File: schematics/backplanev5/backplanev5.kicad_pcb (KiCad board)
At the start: 2 copper layers, 150 x 95 mm, 14 parts, among them J11 Conn_01x02, J12 Conn_01x02, J13 Conn_01x02, J14 Conn_01x02

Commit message: Update V1 fabrication 04-12-2025 JLCPCB
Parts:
- added H1: MountingHole, MountingHole:MountingHole_3.2mm_M3, F.Cu at (20.0, 24.9)
- added H2: MountingHole, MountingHole:MountingHole_3.2mm_M3, F.Cu at (20.0, 115.1)
- added H3: MountingHole, MountingHole:MountingHole_3.2mm_M3, F.Cu at (160.1, 115.1)
- added H4: MountingHole, MountingHole:MountingHole_3.2mm_M3, F.Cu at (160.1, 24.9)
- added H5: MountingHole, MountingHole:MountingHole_3.2mm_M3, F.Cu at (90.0, 24.9)
- added H6: MountingHole, MountingHole:MountingHole_3.2mm_M3, F.Cu at (90.0, 115.1)
- moved J11 12.2 mm to (20.5, 41.1)
- moved J14 10.8 mm to (20.5, 45.0)
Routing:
- net GND: track 874.4 -> 863.4 mm
- net /backplane/+5V: track 490.3 -> 499.6 mm
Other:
- board size 150 x 95 mm -> 150 x 100 mm
- board text added: "/BERR"
- board text added: "/BGACK"
- board text added: "/DEN"
- board text added: "/INTA"
- board text added: "/LDS"
- board text added: "/M1"
- board text added: "/RFSH"
- board text added: "/SS0"
- board text added: "/UDS"
- board text added: "/VMA"
- board text added: "/VPA"
- board text added: "/WAIT"
- board text added: "1"
- board text added: "10"
- board text added: "11"
- board text added: "12"
- board text added: "13"
- board text added: "14"
- board text added: "15"
- board text added: "16"
- board text added: "17"
- board text added: "18"
- board text added: "19"
- board text added: "2"
- board text added: "20"
- board text added: "21"
- board text added: "22"
- board text added: "23"
- board text added: "24"
- board text added: "25"
- board text added: "26"
- board text added: "27"
- board text added: "28"
- board text added: "29"
- board text added: "3"
- board text added: "30"
- board text added: "31"
- board text added: "32"
- board text added: "4"
- board text added: "5"
- board text added: "6"
- board text added: "64"
- board text added: "65"
- board text added: "66"
- board text added: "67"
- board text added: "68"
- board text added: "69"
- board text added: "7"
- board text added: "70"
- board text added: "71"
- board text added: "72"
- board text added: "73"
- board text added: "74"
- board text added: "75"
- board text added: "76"
- board text added: "77"
- board text added: "78"
- board text added: "79"
- board text added: "8"
- board text added: "80"
- board text added: "81"
- board text added: "82"
- board text added: "83"
- board text added: "84"
- board text added: "85"
- board text added: "86"
- board text added: "87"
- board text added: "88"
- board text added: "89"
- board text added: "9"
- board text added: "90"
- board text added: "91"
- board text added: "92"
- board text added: "93"
- board text added: "94"
- board text added: "95"
- board text added: "96"
- board text added: "ALE"
- board text added: "DT/R"
- board text added: "M/IO"
- board text added: "Mod: 09CON"
- board text added: "PDSILVA (C)2549"
- board text added: "Res1"
- board text added: "Res10"
- board text added: "Res11"
- board text added: "Res2"
- board text added: "Res3"
- board text added: "Res4"
- board text added: "Res5"
- board text added: "Res6"
- board text added: "Res7"
- board text added: "Res8"
- board text added: "Res9"
- board text added: "Rev: A 2549"
- board text removed: "MULTI-CPU"
- board text removed: "Res"

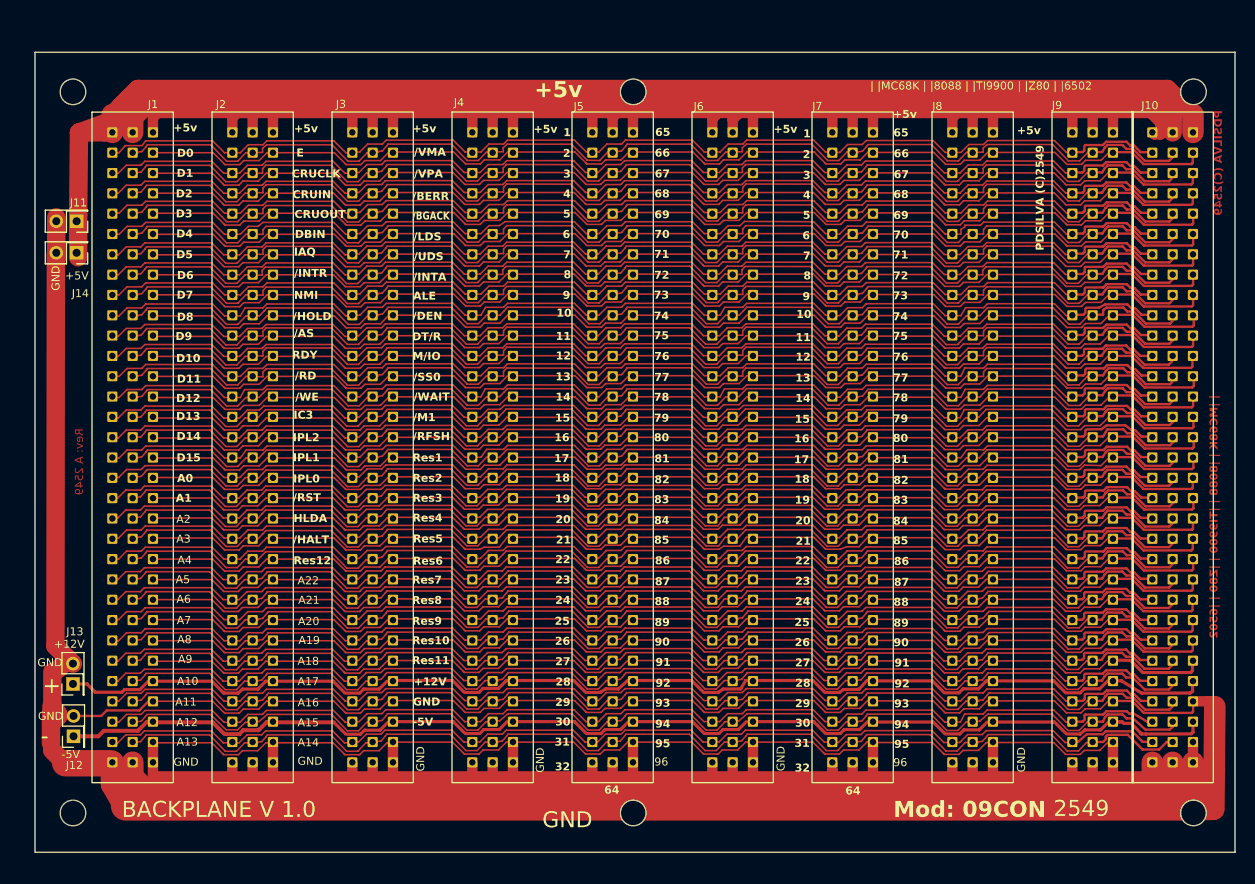
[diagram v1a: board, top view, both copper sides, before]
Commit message: Terminada as mudancas falta agora fazer oDRC
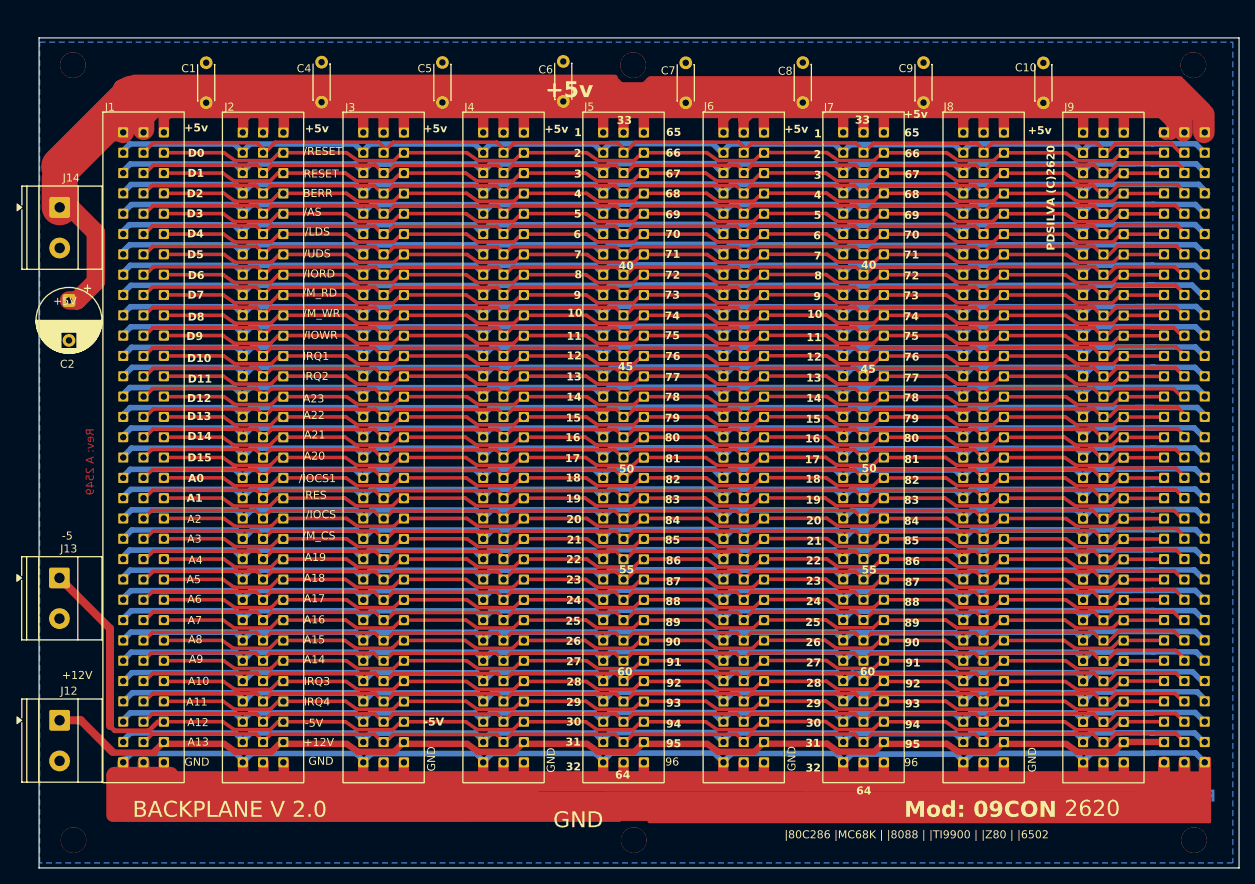
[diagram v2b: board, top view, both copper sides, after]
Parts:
- removed J11: Conn_01x02, Connector_PinHeader_2.54mm:PinHeader_2x01_P2.54mm_Vertical
- added C1: 100nF, Capacitor_THT:C_Disc_D4.3mm_W1.9mm_P5.00mm, F.Cu at (36.6, 26.3)
- added C10: 100nF, Capacitor_THT:C_Disc_D4.3mm_W1.9mm_P5.00mm, F.Cu at (141.3, 26.3)
- added C2: 100uF, Capacitor_THT:CP_Radial_D8.0mm_P5.00mm, F.Cu at (19.5, 51.0)
- added C4: 100nF, Capacitor_THT:C_Disc_D4.3mm_W1.9mm_P5.00mm, F.Cu at (51.1, 26.2)
- added C5: 100nF, Capacitor_THT:C_Disc_D4.3mm_W1.9mm_P5.00mm, F.Cu at (66.2, 26.3)
- added C6: 100nF, Capacitor_THT:C_Disc_D4.3mm_W1.9mm_P5.00mm, F.Cu at (81.3, 26.1)
- added C7: 100nF, Capacitor_THT:C_Disc_D4.3mm_W1.9mm_P5.00mm, F.Cu at (96.6, 26.3)
- added C8: 100nF, Capacitor_THT:C_Disc_D4.3mm_W1.9mm_P5.00mm, F.Cu at (111.2, 26.3)
- added C9: 100nF, Capacitor_THT:C_Disc_D4.3mm_W1.9mm_P5.00mm, F.Cu at (126.3, 26.3)
- J10: moved to B.Cu
- J12, J13, J14: footprint Connector_PinHeader_2.54mm:PinHeader_2x01_P2.54mm_Vertical -> TerminalBlock_Phoenix:TerminalBlock_Phoenix_MKDS-1,5-2-5.08_1x02_P5.08mm_Horizontal
- moved J13 13.4 mm to (18.3, 85.7), turned to -90 degrees
- moved J14 6.06 mm to (18.3, 39.4), turned to -90 degrees
- moved H2 3.40 mm to (20.1, 118.5)
- moved H3 3.40 mm to (160.1, 118.5)
- moved H6 3.40 mm to (90.1, 118.5)
- moved H1 3.34 mm to (20.0, 21.6)
- moved H4 3.34 mm to (160.0, 21.6)
- moved H5 3.34 mm to (90.0, 21.6)
- moved J12 2.65 mm to (18.3, 103.5), turned to -90 degrees
- moved J10 1.47 mm to (158.9, 24.9), turned to 180 degrees
- moved J6 1.39 mm to (103.8, 24.9)
- moved J8 1.37 mm to (133.8, 24.9)
- moved J3 1.37 mm to (58.8, 24.9)
- moved J4 1.36 mm to (73.8, 24.9)
- moved J5 1.36 mm to (88.8, 24.9)
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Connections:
- net /backplane/ALE renamed /backplane//memrd
- net /backplane/CRUCLK renamed /backplane/R2
- net /backplane/CRUIN renamed /backplane/R3
- net /backplane/CRUOUT renamed /backplane/R4
- net /backplane/DBIN renamed /backplane/R5
- net /backplane/DT/R renamed /backplane//iowr
- net /backplane/HLDA renamed /backplane/R19
- net /backplane/IAQ renamed /backplane/R6
- net /backplane/IC3 renamed /backplane/R14
- net /backplane/IPL0 renamed /backplane/R17
- net /backplane/IPL1 renamed /backplane/R16
- net /backplane/IPL2 renamed /backplane/R15
- net /backplane/NMI renamed /backplane/R8
- net /backplane/RDY renamed /backplane/R11
- net /backplane/Res12 renamed /backplane/R21
- net /backplane/Res2 renamed /backplane//IO_CS1
- net /backplane/Res4 renamed /backplane//IO_CS
- net /backplane/Res5 renamed /backplane//MEM_CS
- net /backplane//DEN renamed /backplane//memwr
- net /backplane//HALT renamed /backplane/R20
- net /backplane//HOLD renamed /backplane/R9
- net /backplane//INTA renamed /backplane//iord
- net /backplane//INTR renamed /backplane/R7
- net /backplane//RD renamed /backplane/R12
- net /backplane//RST renamed /backplane/R18
- net /backplane//WAIT renamed /backplane/A23
- net /backplane//WE renamed /backplane/R13
- J1 pad 34: /backplane/E -> /backplane/R1
- J1 pad 43: /backplane//AS -> /backplane/R10
- J1 pad 55: /backplane/A22 -> /backplane/R22
- J1 pad 56: /backplane/A21 -> /backplane/R23
- J1 pad 57: /backplane/A20 -> /backplane/R24
- J1 pad 58: /backplane/A19 -> /backplane/R25
- J1 pad 59: /backplane/A18 -> /backplane/R26
- J1 pad 60: /backplane/A17 -> /backplane/R27
- J1 pad 61: /backplane/A16 -> /backplane/R28
- J1 pad 62: /backplane/A15 -> /backplane/R29
- J1 pad 63: /backplane/A14 -> /backplane/R30
- J1 pad 66: /backplane//VMA -> /backplane//RESET
- J1 pad 67: /backplane//VPA -> /backplane/RESET
- J1 pad 69: /backplane//BGACK -> /backplane//AS
- J1 pad 76: /backplane/M/IO -> /backplane//VMA
- J1 pad 77: /backplane//SSO -> /backplane//VPA
- J1 pad 79: /backplane//M1 -> /backplane/A22
- J1 pad 80: /backplane//RFSH -> /backplane/A21
- J1 pad 81: /backplane/Res1 -> /backplane/A20
- J1 pad 83: /backplane/Res3 -> /backplane/E
- J1 pad 86: /backplane/Res6 -> /backplane/A19
- J1 pad 87: /backplane/Res7 -> /backplane/A18
- J1 pad 88: /backplane/Res8 -> /backplane/A17
- J1 pad 89: /backplane/Res9 -> /backplane/A16
- J1 pad 90: /backplane/Res10 -> /backplane/A15
- J1 pad 91: /backplane/Res11 -> /backplane/A14
- J1 pad 92: /backplane/+12V -> /backplane/R31
- J1 pad 93: GND -> /backplane/R32
- J1 pad 95: GND -> /backplane/+12V
- J10 pad 34: /backplane/E -> /backplane/R1
- J10 pad 43: /backplane//AS -> /backplane/R10
- J10 pad 55: /backplane/A22 -> /backplane/R22
- J10 pad 56: /backplane/A21 -> /backplane/R23
- J10 pad 57: /backplane/A20 -> /backplane/R24
- J10 pad 58: /backplane/A19 -> /backplane/R25
- J10 pad 59: /backplane/A18 -> /backplane/R26
- J10 pad 60: /backplane/A17 -> /backplane/R27
- J10 pad 61: /backplane/A16 -> /backplane/R28
- J10 pad 62: /backplane/A15 -> /backplane/R29
- J10 pad 63: /backplane/A14 -> /backplane/R30
- J10 pad 66: /backplane//VMA -> /backplane//RESET
- J10 pad 67: /backplane//VPA -> /backplane/RESET
- J10 pad 69: /backplane//BGACK -> /backplane//AS
- J10 pad 76: /backplane/M/IO -> /backplane//VMA
- J10 pad 77: /backplane//SSO -> /backplane//VPA
- J10 pad 79: /backplane//M1 -> /backplane/A22
- J10 pad 80: /backplane//RFSH -> /backplane/A21
- J10 pad 81: /backplane/Res1 -> /backplane/A20
- J10 pad 83: /backplane/Res3 -> /backplane/E
- J10 pad 86: /backplane/Res6 -> /backplane/A19
- J10 pad 87: /backplane/Res7 -> /backplane/A18
- J10 pad 88: /backplane/Res8 -> /backplane/A17
- J10 pad 89: /backplane/Res9 -> /backplane/A16
- J10 pad 90: /backplane/Res10 -> /backplane/A15
- J10 pad 91: /backplane/Res11 -> /backplane/A14
- J10 pad 92: /backplane/+12V -> /backplane/R31
- J10 pad 93: GND -> /backplane/R32
- J10 pad 95: GND -> /backplane/+12V
- J12 pad 1: /backplane/-5V -> /backplane/+12V
- J13 pad 1: /backplane/+12V -> /backplane/-5V
- J2 pad 34: /backplane/E -> /backplane/R1
- J2 pad 43: /backplane//AS -> /backplane/R10
- J2 pad 55: /backplane/A22 -> /backplane/R22
- J2 pad 56: /backplane/A21 -> /backplane/R23
- J2 pad 57: /backplane/A20 -> /backplane/R24
- J2 pad 58: /backplane/A19 -> /backplane/R25
- J2 pad 59: /backplane/A18 -> /backplane/R26
- J2 pad 60: /backplane/A17 -> /backplane/R27
- J2 pad 61: /backplane/A16 -> /backplane/R28
- J2 pad 62: /backplane/A15 -> /backplane/R29
- J2 pad 63: /backplane/A14 -> /backplane/R30
- J2 pad 66: /backplane//VMA -> /backplane//RESET
- J2 pad 67: /backplane//VPA -> /backplane/RESET
- J2 pad 69: /backplane//BGACK -> /backplane//AS
- J2 pad 76: /backplane/M/IO -> /backplane//VMA
- J2 pad 77: /backplane//SSO -> /backplane//VPA
- J2 pad 79: /backplane//M1 -> /backplane/A22
- J2 pad 80: /backplane//RFSH -> /backplane/A21
- J2 pad 81: /backplane/Res1 -> /backplane/A20
- J2 pad 83: /backplane/Res3 -> /backplane/E
- J2 pad 86: /backplane/Res6 -> /backplane/A19
- J2 pad 87: /backplane/Res7 -> /backplane/A18
- J2 pad 88: /backplane/Res8 -> /backplane/A17
- J2 pad 89: /backplane/Res9 -> /backplane/A16
- J2 pad 90: /backplane/Res10 -> /backplane/A15
- J2 pad 91: /backplane/Res11 -> /backplane/A14
- J2 pad 92: /backplane/+12V -> /backplane/R31
- J2 pad 93: GND -> /backplane/R32
- J2 pad 95: GND -> /backplane/+12V
- J3 pad 34: /backplane/E -> /backplane/R1
- J3 pad 43: /backplane//AS -> /backplane/R10
- J3 pad 55: /backplane/A22 -> /backplane/R22
- J3 pad 56: /backplane/A21 -> /backplane/R23
- J3 pad 57: /backplane/A20 -> /backplane/R24
- J3 pad 58: /backplane/A19 -> /backplane/R25
- J3 pad 59: /backplane/A18 -> /backplane/R26
- J3 pad 60: /backplane/A17 -> /backplane/R27
- J3 pad 61: /backplane/A16 -> /backplane/R28
- J3 pad 62: /backplane/A15 -> /backplane/R29
- J3 pad 63: /backplane/A14 -> /backplane/R30
- J3 pad 66: /backplane//VMA -> /backplane//RESET
- J3 pad 67: /backplane//VPA -> /backplane/RESET
- J3 pad 69: /backplane//BGACK -> /backplane//AS
- J3 pad 76: /backplane/M/IO -> /backplane//VMA
- J3 pad 77: /backplane//SSO -> /backplane//VPA
- J3 pad 79: /backplane//M1 -> /backplane/A22
- J3 pad 80: /backplane//RFSH -> /backplane/A21
- J3 pad 81: /backplane/Res1 -> /backplane/A20
- J3 pad 83: /backplane/Res3 -> /backplane/E
- J3 pad 86: /backplane/Res6 -> /backplane/A19
- J3 pad 87: /backplane/Res7 -> /backplane/A18
- J3 pad 88: /backplane/Res8 -> /backplane/A17
- J3 pad 89: /backplane/Res9 -> /backplane/A16
- J3 pad 90: /backplane/Res10 -> /backplane/A15
- J3 pad 91: /backplane/Res11 -> /backplane/A14
- J3 pad 92: /backplane/+12V -> /backplane/R31
- J3 pad 93: GND -> /backplane/R32
- J3 pad 95: GND -> /backplane/+12V
- J4 pad 34: /backplane/E -> /backplane/R1
- J4 pad 43: /backplane//AS -> /backplane/R10
- J4 pad 55: /backplane/A22 -> /backplane/R22
- J4 pad 56: /backplane/A21 -> /backplane/R23
- J4 pad 57: /backplane/A20 -> /backplane/R24
- J4 pad 58: /backplane/A19 -> /backplane/R25
- J4 pad 59: /backplane/A18 -> /backplane/R26
- J4 pad 60: /backplane/A17 -> /backplane/R27
- J4 pad 61: /backplane/A16 -> /backplane/R28
- J4 pad 62: /backplane/A15 -> /backplane/R29
- J4 pad 63: /backplane/A14 -> /backplane/R30
- J4 pad 66: /backplane//VMA -> /backplane//RESET
- J4 pad 67: /backplane//VPA -> /backplane/RESET
- J4 pad 69: /backplane//BGACK -> /backplane//AS
- J4 pad 76: /backplane/M/IO -> /backplane//VMA
- J4 pad 77: /backplane//SSO -> /backplane//VPA
- J4 pad 79: /backplane//M1 -> /backplane/A22
- J4 pad 80: /backplane//RFSH -> /backplane/A21
- J4 pad 81: /backplane/Res1 -> /backplane/A20
- J4 pad 83: /backplane/Res3 -> /backplane/E
- J4 pad 86: /backplane/Res6 -> /backplane/A19
- J4 pad 87: /backplane/Res7 -> /backplane/A18
- J4 pad 88: /backplane/Res8 -> /backplane/A17
- J4 pad 89: /backplane/Res9 -> /backplane/A16
- J4 pad 90: /backplane/Res10 -> /backplane/A15
- J4 pad 91: /backplane/Res11 -> /backplane/A14
- J4 pad 92: /backplane/+12V -> /backplane/R31
- J4 pad 93: GND -> /backplane/R32
- J4 pad 95: GND -> /backplane/+12V
- J5 pad 34: /backplane/E -> /backplane/R1
- J5 pad 43: /backplane//AS -> /backplane/R10
- J5 pad 55: /backplane/A22 -> /backplane/R22
- J5 pad 56: /backplane/A21 -> /backplane/R23
- J5 pad 57: /backplane/A20 -> /backplane/R24
- J5 pad 58: /backplane/A19 -> /backplane/R25
- J5 pad 59: /backplane/A18 -> /backplane/R26
- J5 pad 60: /backplane/A17 -> /backplane/R27
- J5 pad 61: /backplane/A16 -> /backplane/R28
- J5 pad 62: /backplane/A15 -> /backplane/R29
- J5 pad 63: /backplane/A14 -> /backplane/R30
- J5 pad 66: /backplane//VMA -> /backplane//RESET
- J5 pad 67: /backplane//VPA -> /backplane/RESET
- J5 pad 69: /backplane//BGACK -> /backplane//AS
- J5 pad 76: /backplane/M/IO -> /backplane//VMA
- J5 pad 77: /backplane//SSO -> /backplane//VPA
- J5 pad 79: /backplane//M1 -> /backplane/A22
- J5 pad 80: /backplane//RFSH -> /backplane/A21
- J5 pad 81: /backplane/Res1 -> /backplane/A20
- J5 pad 83: /backplane/Res3 -> /backplane/E
- J5 pad 86: /backplane/Res6 -> /backplane/A19
- J5 pad 87: /backplane/Res7 -> /backplane/A18
- J5 pad 88: /backplane/Res8 -> /backplane/A17
- J5 pad 89: /backplane/Res9 -> /backplane/A16
- J5 pad 90: /backplane/Res10 -> /backplane/A15
- J5 pad 91: /backplane/Res11 -> /backplane/A14
- J5 pad 92: /backplane/+12V -> /backplane/R31
- J5 pad 93: GND -> /backplane/R32
- J5 pad 95: GND -> /backplane/+12V
- J6 pad 34: /backplane/E -> /backplane/R1
- J6 pad 43: /backplane//AS -> /backplane/R10
- J6 pad 55: /backplane/A22 -> /backplane/R22
- J6 pad 56: /backplane/A21 -> /backplane/R23
- J6 pad 57: /backplane/A20 -> /backplane/R24
- J6 pad 58: /backplane/A19 -> /backplane/R25
- J6 pad 59: /backplane/A18 -> /backplane/R26
- J6 pad 60: /backplane/A17 -> /backplane/R27
- J6 pad 61: /backplane/A16 -> /backplane/R28
- J6 pad 62: /backplane/A15 -> /backplane/R29
- J6 pad 63: /backplane/A14 -> /backplane/R30
- J6 pad 66: /backplane//VMA -> /backplane//RESET
- J6 pad 67: /backplane//VPA -> /backplane/RESET
- J6 pad 69: /backplane//BGACK -> /backplane//AS
- J6 pad 76: /backplane/M/IO -> /backplane//VMA
- J6 pad 77: /backplane//SSO -> /backplane//VPA
- J6 pad 79: /backplane//M1 -> /backplane/A22
- J6 pad 80: /backplane//RFSH -> /backplane/A21
- J6 pad 81: /backplane/Res1 -> /backplane/A20
- J6 pad 83: /backplane/Res3 -> /backplane/E
- J6 pad 86: /backplane/Res6 -> /backplane/A19
- J6 pad 87: /backplane/Res7 -> /backplane/A18
- J6 pad 88: /backplane/Res8 -> /backplane/A17
- J6 pad 89: /backplane/Res9 -> /backplane/A16
- J6 pad 90: /backplane/Res10 -> /backplane/A15
- J6 pad 91: /backplane/Res11 -> /backplane/A14
- J6 pad 92: /backplane/+12V -> /backplane/R31
- J6 pad 93: GND -> /backplane/R32
- J6 pad 95: GND -> /backplane/+12V
- J7 pad 34: /backplane/E -> /backplane/R1
- J7 pad 43: /backplane//AS -> /backplane/R10
- J7 pad 55: /backplane/A22 -> /backplane/R22
- J7 pad 56: /backplane/A21 -> /backplane/R23
- J7 pad 57: /backplane/A20 -> /backplane/R24
- J7 pad 58: /backplane/A19 -> /backplane/R25
- J7 pad 59: /backplane/A18 -> /backplane/R26
- J7 pad 60: /backplane/A17 -> /backplane/R27
- J7 pad 61: /backplane/A16 -> /backplane/R28
- J7 pad 62: /backplane/A15 -> /backplane/R29
- J7 pad 63: /backplane/A14 -> /backplane/R30
- J7 pad 66: /backplane//VMA -> /backplane//RESET
- J7 pad 67: /backplane//VPA -> /backplane/RESET
- J7 pad 69: /backplane//BGACK -> /backplane//AS
- J7 pad 76: /backplane/M/IO -> /backplane//VMA
- J7 pad 77: /backplane//SSO -> /backplane//VPA
- J7 pad 79: /backplane//M1 -> /backplane/A22
- J7 pad 80: /backplane//RFSH -> /backplane/A21
- J7 pad 81: /backplane/Res1 -> /backplane/A20
- J7 pad 83: /backplane/Res3 -> /backplane/E
- J7 pad 86: /backplane/Res6 -> /backplane/A19
- J7 pad 87: /backplane/Res7 -> /backplane/A18
- J7 pad 88: /backplane/Res8 -> /backplane/A17
- J7 pad 89: /backplane/Res9 -> /backplane/A16
- J7 pad 90: /backplane/Res10 -> /backplane/A15
- J7 pad 91: /backplane/Res11 -> /backplane/A14
- J7 pad 92: /backplane/+12V -> /backplane/R31
- J7 pad 93: GND -> /backplane/R32
- J7 pad 95: GND -> /backplane/+12V
- J8 pad 34: /backplane/E -> /backplane/R1
- J8 pad 43: /backplane//AS -> /backplane/R10
- J8 pad 55: /backplane/A22 -> /backplane/R22
- J8 pad 56: /backplane/A21 -> /backplane/R23
- J8 pad 57: /backplane/A20 -> /backplane/R24
- J8 pad 58: /backplane/A19 -> /backplane/R25
- J8 pad 59: /backplane/A18 -> /backplane/R26
- J8 pad 60: /backplane/A17 -> /backplane/R27
- J8 pad 61: /backplane/A16 -> /backplane/R28
- J8 pad 62: /backplane/A15 -> /backplane/R29
- J8 pad 63: /backplane/A14 -> /backplane/R30
- J8 pad 66: /backplane//VMA -> /backplane//RESET
- J8 pad 67: /backplane//VPA -> /backplane/RESET
- J8 pad 69: /backplane//BGACK -> /backplane//AS
- J8 pad 76: /backplane/M/IO -> /backplane//VMA
- J8 pad 77: /backplane//SSO -> /backplane//VPA
- J8 pad 79: /backplane//M1 -> /backplane/A22
- J8 pad 80: /backplane//RFSH -> /backplane/A21
- J8 pad 81: /backplane/Res1 -> /backplane/A20
- J8 pad 83: /backplane/Res3 -> /backplane/E
- J8 pad 86: /backplane/Res6 -> /backplane/A19
- J8 pad 87: /backplane/Res7 -> /backplane/A18
- J8 pad 88: /backplane/Res8 -> /backplane/A17
- J8 pad 89: /backplane/Res9 -> /backplane/A16
- J8 pad 90: /backplane/Res10 -> /backplane/A15
- J8 pad 91: /backplane/Res11 -> /backplane/A14
- J8 pad 92: /backplane/+12V -> /backplane/R31
- J8 pad 93: GND -> /backplane/R32
- J8 pad 95: GND -> /backplane/+12V
- J9 pad 34: /backplane/E -> /backplane/R1
- J9 pad 43: /backplane//AS -> /backplane/R10
- J9 pad 55: /backplane/A22 -> /backplane/R22
- J9 pad 56: /backplane/A21 -> /backplane/R23
- J9 pad 57: /backplane/A20 -> /backplane/R24
- J9 pad 58: /backplane/A19 -> /backplane/R25
- J9 pad 59: /backplane/A18 -> /backplane/R26
- J9 pad 60: /backplane/A17 -> /backplane/R27
- J9 pad 61: /backplane/A16 -> /backplane/R28
- J9 pad 62: /backplane/A15 -> /backplane/R29
- J9 pad 63: /backplane/A14 -> /backplane/R30
- J9 pad 66: /backplane//VMA -> /backplane//RESET
- J9 pad 67: /backplane//VPA -> /backplane/RESET
- J9 pad 69: /backplane//BGACK -> /backplane//AS
- J9 pad 76: /backplane/M/IO -> /backplane//VMA
- J9 pad 77: /backplane//SSO -> /backplane//VPA
- J9 pad 79: /backplane//M1 -> /backplane/A22
- J9 pad 80: /backplane//RFSH -> /backplane/A21
- J9 pad 81: /backplane/Res1 -> /backplane/A20
- J9 pad 83: /backplane/Res3 -> /backplane/E
- J9 pad 86: /backplane/Res6 -> /backplane/A19
- J9 pad 87: /backplane/Res7 -> /backplane/A18
- J9 pad 88: /backplane/Res8 -> /backplane/A17
- J9 pad 89: /backplane/Res9 -> /backplane/A16
- J9 pad 90: /backplane/Res10 -> /backplane/A15
- J9 pad 91: /backplane/Res11 -> /backplane/A14
- J9 pad 92: /backplane/+12V -> /backplane/R31
- J9 pad 93: GND -> /backplane/R32
- J9 pad 95: GND -> /backplane/+12V
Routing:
- net GND: track 863.4 -> 598.4 mm
- net /backplane/Res1: track 141.9 -> 0.00 mm
- net /backplane/Res3: track 141.9 -> 0.00 mm
- net /backplane/Res10: track 141.9 -> 0.00 mm
- net /backplane/M/IO: track 141.9 -> 0.00 mm
- net /backplane/Res9: track 141.9 -> 0.00 mm
- net /backplane/Res8: track 141.9 -> 0.00 mm
- net /backplane//SSO: track 141.9 -> 0.00 mm
- net /backplane//RFSH: track 141.9 -> 0.00 mm
- net /backplane//BGACK: track 141.9 -> 0.00 mm
- net /backplane/Res7: track 141.9 -> 0.00 mm
- net /backplane/Res6: track 141.9 -> 0.00 mm
- net /backplane//M1: track 141.9 -> 0.00 mm
- net /backplane/Res11: track 141.8 -> 0.00 mm
- net /backplane/R1: track 0.00 -> 138.9 mm
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- added copper zone on B.Cu, net GND
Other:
- board size 150 x 100 mm -> 150 x 103.8 mm
- board text added: "-5"
- board text added: "/IOCS"
- board text added: "/IOCS1"
- board text added: "/IORD"
- board text added: "/IOWR"
- board text added: "/M_CS"
- board text added: "/M_RD"
- board text added: "/M_WR"
- board text added: "/RESET"
- board text added: "2620"
- board text added: "33"
- board text added: "40"
- board text added: "45"
- board text added: "50"
- board text added: "55"
- board text added: "60"
- board text added: "A23"
- board text added: "BACKPLANE V 2.0"
- board text added: "BERR"
- board text added: "IRQ1"
- board text added: "IRQ2"
- board text added: "IRQ3"
- board text added: "IRQ4"
- board text added: "PDSILVA (C)2620"
- board text added: "RES"
- board text added: "RESET"
- board text added: "REV.B"
- board text added: "pdsilva 2620"
- board text added: "|80C286 |MC68K | |8088 | |TI9900 | |Z80 | |6502"
- board text removed: "+"
- board text removed: "-"
- board text removed: "/BERR"
- board text removed: "/BGACK"
- board text removed: "/DEN"
- board text removed: "/HALT"
- board text removed: "/HOLD"
- board text removed: "/INTA"
- board text removed: "/INTR"
- board text removed: "/M1"
- board text removed: "/RD"
- board text removed: "/RFSH"
- board text removed: "/RST"
- board text removed: "/SS0"
- board text removed: "/VMA"
- board text removed: "/VPA"
- board text removed: "/WAIT"
- board text removed: "/WE"
- board text removed: "2549"
- board text removed: "ALE"
- board text removed: "BACKPLANE V 1.0"
- board text removed: "CRUCLK"
- board text removed: "CRUIN"
- board text removed: "CRUOUT"
- board text removed: "DBIN"
- board text removed: "DT/R"
- board text removed: "E"
- board text removed: "HLDA"
- board text removed: "IAQ"
- board text removed: "IC3"
- board text removed: "IPL0"
- board text removed: "IPL1"
- board text removed: "IPL2"
- board text removed: "M/IO"
- board text removed: "NMI"
- board text removed: "PDSILVA (C)2549"
- board text removed: "RDY"
- board text removed: "Res1"
- board text removed: "Res10"
- board text removed: "Res11"
- board text removed: "Res12"
- board text removed: "Res2"
- board text removed: "Res3"
- board text removed: "Res4"
- board text removed: "Res5"
- board text removed: "Res6"
- board text removed: "Res7"
- board text removed: "Res8"
- board text removed: "Res9"
- board text removed: "| |MC68K | |8088 | |TI9900 | |Z80 | |6502"

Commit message: Terminado o DRC
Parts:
- moved J12 17.8 mm to (18.3, 85.7)
- moved J13 17.8 mm to (18.3, 103.4)
- moved C4 0.47 mm to (51.5, 26.5)
- moved J14 0.07 mm to (18.3, 39.4)
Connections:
- C4 pad 1: unconnected-(C4-Pad1) -> /backplane/+5V
- C4 pad 2: unconnected-(C4-Pad2) -> GND
- C5 pad 1: unconnected-(C5-Pad1) -> /backplane/+5V
- C5 pad 2: unconnected-(C5-Pad2) -> GND
- J12 pad 1: /backplane/+12V -> /backplane/-5V
- J13 pad 1: /backplane/-5V -> /backplane/+12V
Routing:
- net /backplane/+5V: track 506.5 -> 236.4 mm
- net /backplane/A8: track 142.4 -> 145.1 mm
- net /backplane/A10: track 143.0 -> 145.6 mm
- net /backplane/A9: track 142.7 -> 145.1 mm
- net /backplane/A11: track 142.7 -> 145.0 mm
- net /backplane/D8: track 142.7 -> 144.4 mm
- net /backplane/A12: track 142.7 -> 144.4 mm
- net /backplane/D10: track 142.7 -> 144.3 mm
- net /backplane/D11: track 142.7 -> 144.0 mm
- net /backplane/A0: track 142.7 -> 144.0 mm
- net /backplane/A2: track 142.7 -> 144.0 mm
- net /backplane/D9: track 142.7 -> 144.0 mm
- net /backplane/A13: track 142.7 -> 143.9 mm
- net /backplane/D12: track 142.7 -> 143.9 mm
- net /backplane/A3: track 142.7 -> 143.8 mm
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- added copper zone on F.Cu, net /backplane/+5V
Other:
- board size 150 x 103.8 mm -> 150 x 102.7 mm

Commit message: Versao em producao
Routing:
- net /backplane/+5V: track 236.4 -> 240.3 mm
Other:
- board text added: "Mod: PDS112 09CON"
- board text added: "Rev: B 2620"
- board text added: "SN:"
- board text removed: "Mod: 09CON"
- board text removed: "Rev: A 2549"
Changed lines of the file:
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@@
 		(tenting front back)
 		(pcbplotparams
-			(layerselection 0x00000000_00000000_55555555_575555ff)
+			(layerselection 0x00000000_00000000_55555555_5755557f)
 			(plot_on_all_layers_selection 0x00000000_00000000_00000000_00000000)
 			(disableapertmacros no)
@@
 	)
 	(gr_rect
+		(start 56.43 116.27)
+		(end 79.24 119.34)
+		(stroke
+			(width 0.1)
+			(type default)
+		)
+		(fill no)
+		(layer "F.SilkS")
+	)
+	(gr_rect
 		(start 15.06 18.6964)
 		(end 165.03 121.3556)
@@
 		(layer "Edge.Cuts")
 	)
-	(gr_text "Rev: A 2549"
+	(gr_text "Rev: B 2620"
 		(at 22.72 66.99 90)
 		(layer "F.Cu")
@@
 		)
 	)
-	(gr_text "64"
-		(at 87.76 110.89 0)
+	(gr_text "45\n"
+		(at 87.58 59.85 0)
 		(layer "F.SilkS")
 		(effects
@@
 		)
 	)
-	(gr_text "33"
-		(at 87.97 29.07 0)
+	(gr_text "40"
+		(at 87.64 47.16 0)
 		(layer "F.SilkS")
 		(effects
@@
 	)
 	(gr_text "60\n"
-		(at 88.04 98.01 0)
+		(at 87.66 97.93 0)
 		(layer "F.SilkS")
 		(effects
@@
 		)
 	)
-	(gr_text "45\n"
-		(at 88.12 59.85 0)
+	(gr_text "50"
+		(at 87.73 72.57 0)
 		(layer "F.SilkS")
 		(effects
@@
 		)
 	)
-	(gr_text "40"
-		(at 88.2 47.26 0)
+	(gr_text "64"
+		(at 87.76 110.89 0)
 		(layer "F.SilkS")
 		(effects
@@
 		)
 	)
-	(gr_text "50"
-		(at 88.25 72.65 0)
+	(gr_text "33"
+		(at 87.97 29.07 0)
 		(layer "F.SilkS")
 		(effects
@@
 		)
 	)
-	(gr_text "33"
-		(at 117.73 29.02 0)
+	(gr_text "45\n"
+		(at 117.52 59.86 0)
 		(layer "F.SilkS")
 		(effects
@@
 		)
 	)
-	(gr_text "64"
-		(at 117.9 112.88 0)
+	(gr_text "33"
+		(at 117.73 29.02 0)
 		(layer "F.SilkS")
 		(effects
@@
 		)
 	)
-	(gr_text "60\n"
-		(at 118.36 97.99 0)
+	(gr_text "64"
+		(at 117.9 112.88 0)
 		(layer "F.SilkS")
 		(effects
@@
 		)
 	)
-	(gr_text "45\n"
-		(at 118.44 60.17 0)
+	(gr_text "60\n"
+		(at 118.36 97.96 0)
 		(layer "F.SilkS")
 		(effects
@@
 	)
 	(gr_text "+5v"
-		(at 77.42 18.69 0)
+		(at 71.79 25.44 0)
 		(layer "F.SilkS")
 		(effects
@@
 		)
 	)
-	(gr_text "Mod: 09CON"
-		(at 123.9 115.8 0)
+	(gr_text "SN:"
+		(at 56.43 119 0)
 		(layer "F.SilkS")
 		(effects
 			(font
 				(size 2 2)
-				(thickness 0.2)
+				(thickness 0.4)
+				(bold yes)
+			)
+			(justify left bottom)
+		)
+	)
+	(gr_text "Mod: PDS112 09CON"
+		(at 108.99 115.8 0)
+		(layer "F.SilkS")
+		(effects
+			(font
+				(size 2 2)
+				(thickness 0.5)
 				(bold yes)
 			)
@@
 	)
 	(segment
+		(start 18.72 29.97)
+		(end 26.14 25.28)
+		(width 5)
+		(layer "F.Cu")
+		(net 61)
+	)
+	(segment
 		(start 56.28 30)
 		(end 56.28 27.67)
@@
 		(start 22.86 42.52)
 		(end 22.86 48.65)
-		(width 2.3)
+		(width 3)
 		(layer "F.Cu")
 		(net 61)
@@
 	)
 	(segment
-		(start 18.46 32.96)
-		(end 26.14 25.28)
-		(width 5)
-		(layer "F.Cu")
-		(net 61)
-	)
-	(segment
 		(start 151.36 30)
 		(end 151.36 27.7)
@@
 		(start 22.86 48.65)
 		(end 20.51 51)
-		(width 2.3)
+		(width 3)
 		(layer "F.Cu")
 		(net 61)
@@
 	)
 	(segment
+		(start 18.26901 30.42099)
+		(end 18.72 29.97)
+		(width 2.3)
+		(layer "F.Cu")
+		(net 61)
+	)
+	(segment
 		(start 19.71 39.37)
 		(end 22.86 42.52)
-		(width 2.3)
+		(width 3)
 		(layer "F.Cu")
 		(net 61)
@@
 	)
 	(segment
-		(start 18.34 36.39)
-		(end 18.34 32.74)
-		(width 4.5)
+		(start 18.26901 39.37)
+		(end 18.26901 30.42099)
+		(width 5)
 		(layer "F.Cu")
 		(net 61)
@@
 		(layer "F.Cu")
 		(net 65)
-	)
-	(segment
-		(start 24.93 107.44)
-		(end 24.99 107.38)
-		(width 0.4)
-		(layer "F.Cu")
-		(net 65)

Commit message: CONSTRAINTS 02 UPDATING
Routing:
- net /backplane/R26: track 137.4 -> 135.1 mm
- net /backplane/R29: track 137.6 -> 135.6 mm
- net /backplane/R21: track 137.4 -> 135.5 mm
- net /backplane/R28: track 137.4 -> 135.6 mm
- net /backplane/R17: track 137.4 -> 135.6 mm
- net /backplane/R16: track 137.4 -> 135.7 mm
- net /backplane/R8: track 137.4 -> 135.7 mm
- net /backplane/R27: track 137.4 -> 135.7 mm
- net /backplane/R23: track 137.6 -> 135.9 mm
- net /backplane/R6: track 137.4 -> 135.7 mm
- net /backplane/R25: track 137.9 -> 136.3 mm
- net /backplane/R19: track 137.4 -> 135.8 mm
- net /backplane/R13: track 137.5 -> 135.9 mm
- net /backplane/R24: track 137.3 -> 135.7 mm
- net /backplane/R30: track 137.7 -> 136.2 mm
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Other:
- board text added: "Fab: fix 01"

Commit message: Enviado arquivo Gerber_fab_2620_02.zip para TEC-CI
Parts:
- renumbered J14 to J11
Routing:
- net /backplane/R23: track 135.9 -> 134.9 mm
- net /backplane/R29: track 135.6 -> 134.7 mm
- net /backplane/R19: track 135.8 -> 134.9 mm
- net /backplane/R7: track 136.7 -> 135.8 mm
- net /backplane/R5: track 136.5 -> 135.7 mm
- net /backplane/R6: track 135.7 -> 134.9 mm
- net /backplane/R12: track 136.3 -> 135.5 mm
- net /backplane/R17: track 135.6 -> 134.9 mm
- net /backplane/R25: track 136.3 -> 135.5 mm
- net /backplane/R16: track 135.7 -> 134.9 mm
- net /backplane/R30: track 136.2 -> 135.4 mm
- net /backplane/R11: track 136.4 -> 135.6 mm
- net /backplane/R22: track 136.0 -> 135.2 mm
- net /backplane/R8: track 135.7 -> 134.9 mm
- net /backplane/R27: track 135.7 -> 135.0 mm
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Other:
- board text added: "Fab: fix 02"
- board text removed: "Fab: fix 01"
